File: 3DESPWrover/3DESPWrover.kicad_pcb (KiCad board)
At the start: 2 copper layers, 40 x 40 mm, 23 parts, among them J1 Conn_01x05_Male, J2 Conn_01x03_Female, J3 Conn_02x03_Odd_Even, J4 Conn_02x07_Odd_Even, SW1 SW_Push, SW2 SW_Push, U1 ESP32-S2-WROVER

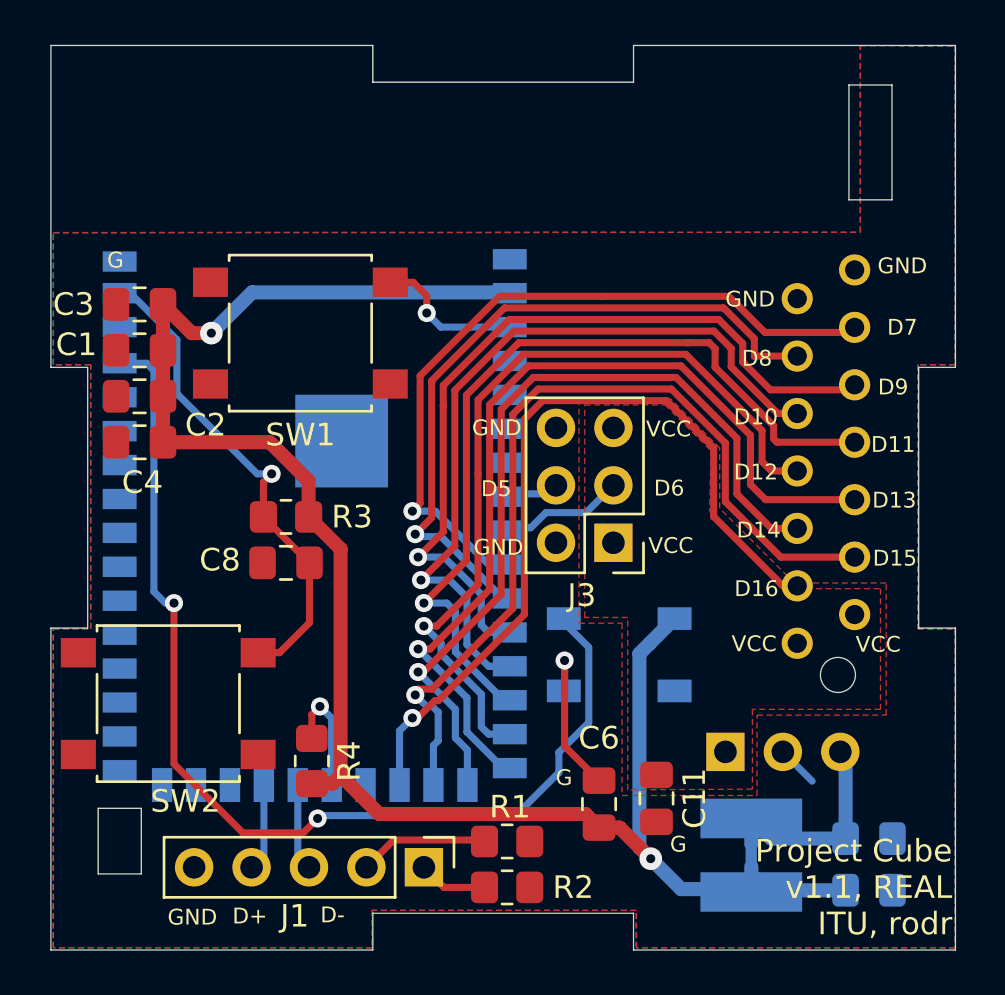
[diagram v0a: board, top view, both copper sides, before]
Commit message: Replaced TE connector and regulator to smd on top board
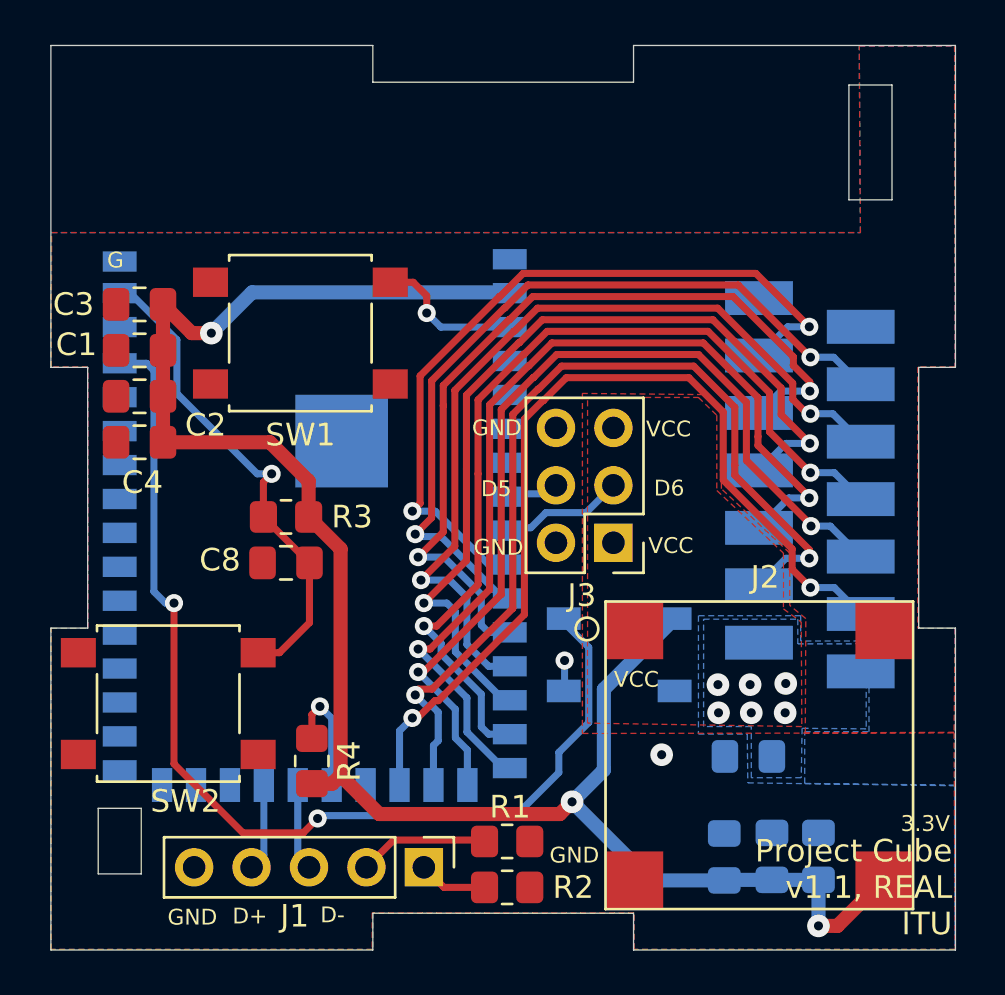
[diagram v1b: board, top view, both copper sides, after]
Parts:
- removed L1: 10u, Custom:L_4.5x4_H3.2
- removed NT1: Net-Tie_2, NetTie:NetTie-2_SMD_Pad0.5mm
- C11, C6: moved to B.Cu
- J2: value Conn_01x03_Female -> Conn_01x04; footprint Connector_PinHeader_2.54mm:PinHeader_1x03_P2.54mm_Vertical -> Custom:K7803JT-500R3-SMD; moved to F.Cu
- J4: footprint Custom:TE_Micromatch_2,54_14 -> Custom:TE_Micromatch_2,54_14_SMD
- moved J4 9.70 mm to (233.5, 69.4)
- moved C6 6.01 mm to (229.7, 85.9)
- moved C11 4.47 mm to (230.8, 81.5), turned to 180 degrees
- moved C9 4.36 mm to (231.8, 85.9), turned to 90 degrees
- moved C10 2.69 mm to (233.9, 85.9), turned to 90 degrees
- moved J2 1.51 mm to (231.2, 81.4), turned to 0 degrees
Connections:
- C9 pad 1: /Vout -> +3V3
- J2 pad 3: /Vout -> +3V3
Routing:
- net /Vout: track 10.3 -> 0.00 mm
- net GND: track 9.39 -> 1.62 mm, vias 1 -> 2
- net /D16: track 36.3 -> 40.9 mm, vias 1 -> 2
- net /D12: track 36.1 -> 40.5 mm, vias 1 -> 2
- net /D14: track 37.1 -> 41.3 mm, vias 1 -> 2
- net /D10: track 34.0 -> 38.1 mm, vias 1 -> 2
- net /D8: track 31.6 -> 35.3 mm, vias 1 -> 2
- net /D15: track 39.4 -> 41.4 mm, vias 1 -> 2
- net /D13: track 40.1 -> 41.7 mm, vias 1 -> 2
- net /D9: track 35.5 -> 37.0 mm, vias 1 -> 2
- net /D7: track 32.8 -> 34.2 mm, vias 1 -> 2
- net +3V3: track 82.9 -> 84.3 mm, vias 2 -> 3
- net /D11: track 37.6 -> 38.9 mm, vias 1 -> 2
- net /Vin: vias 0 -> 6
- added copper zone on B.Cu, net /Vin
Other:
- board text added: "Project Cube v1.1, REAL ITU"
- board text removed: "Project Cube v1.1, REAL ITU, rodr"
